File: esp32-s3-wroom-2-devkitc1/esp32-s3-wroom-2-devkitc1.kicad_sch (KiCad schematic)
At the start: 1 part

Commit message: net class plus cleanup
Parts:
- RFM95W1: footprint maciek-lib:lora-adafruit -> lora-adafruit
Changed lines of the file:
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@@
+		)
+	)
+	(netclass_flag ""
+		(length 2.54)
+		(shape round)
+		(at 107.95 88.9 0)
+		(fields_autoplaced yes)
+		(effects
+			(font
+				(size 1.27 1.27)
+			)
+			(justify left bottom)
+		)
+		(property "Netclass" "POWER"
+			(at 108.6485 86.36 0)
+			(effects
+				(font
+					(size 1.27 1.27)
+					(italic yes)
+				)
+				(justify left)
+			)
+		)
+	)
+	(netclass_flag ""
+		(length 2.54)
+		(shape round)
+		(at 107.95 86.36 0)
+		(fields_autoplaced yes)
+		(effects
+			(font
+				(size 1.27 1.27)
+			)
+			(justify left bottom)
+		)
+		(property "Netclass" "POWER"
+			(at 108.6485 83.82 0)
+			(effects
+				(font
+					(size 1.27 1.27)
+					(italic yes)
+				)
+				(justify left)
+			)
 		)
 	)
@@
 			)
 		)
-		(property "Footprint" "maciek-lib:lora-adafruit"
+		(property "Footprint" "lora-adafruit"
 			(at 132.08 106.68 0)
 			(effects

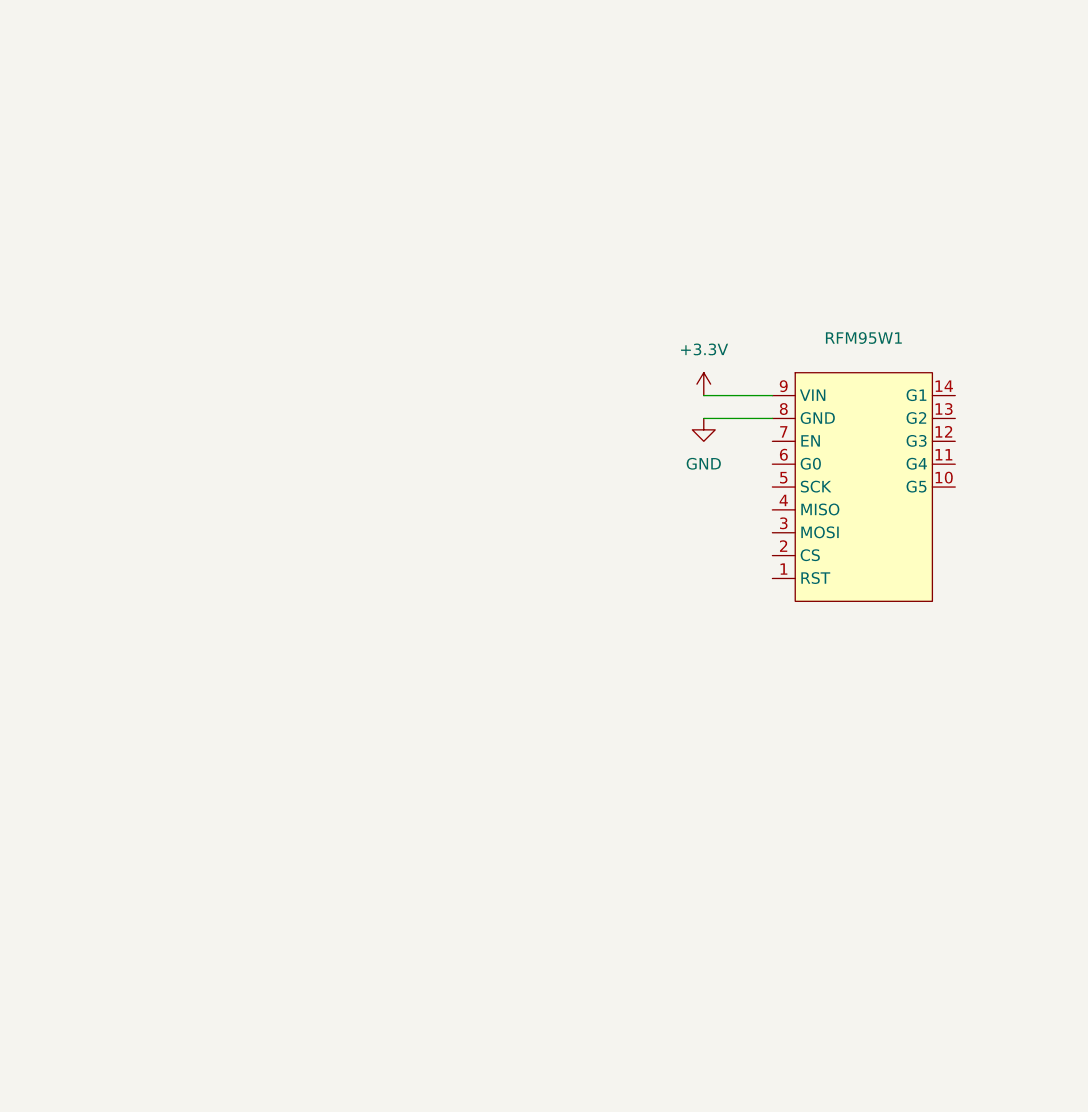
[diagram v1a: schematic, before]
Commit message: add nests and 3v3 area
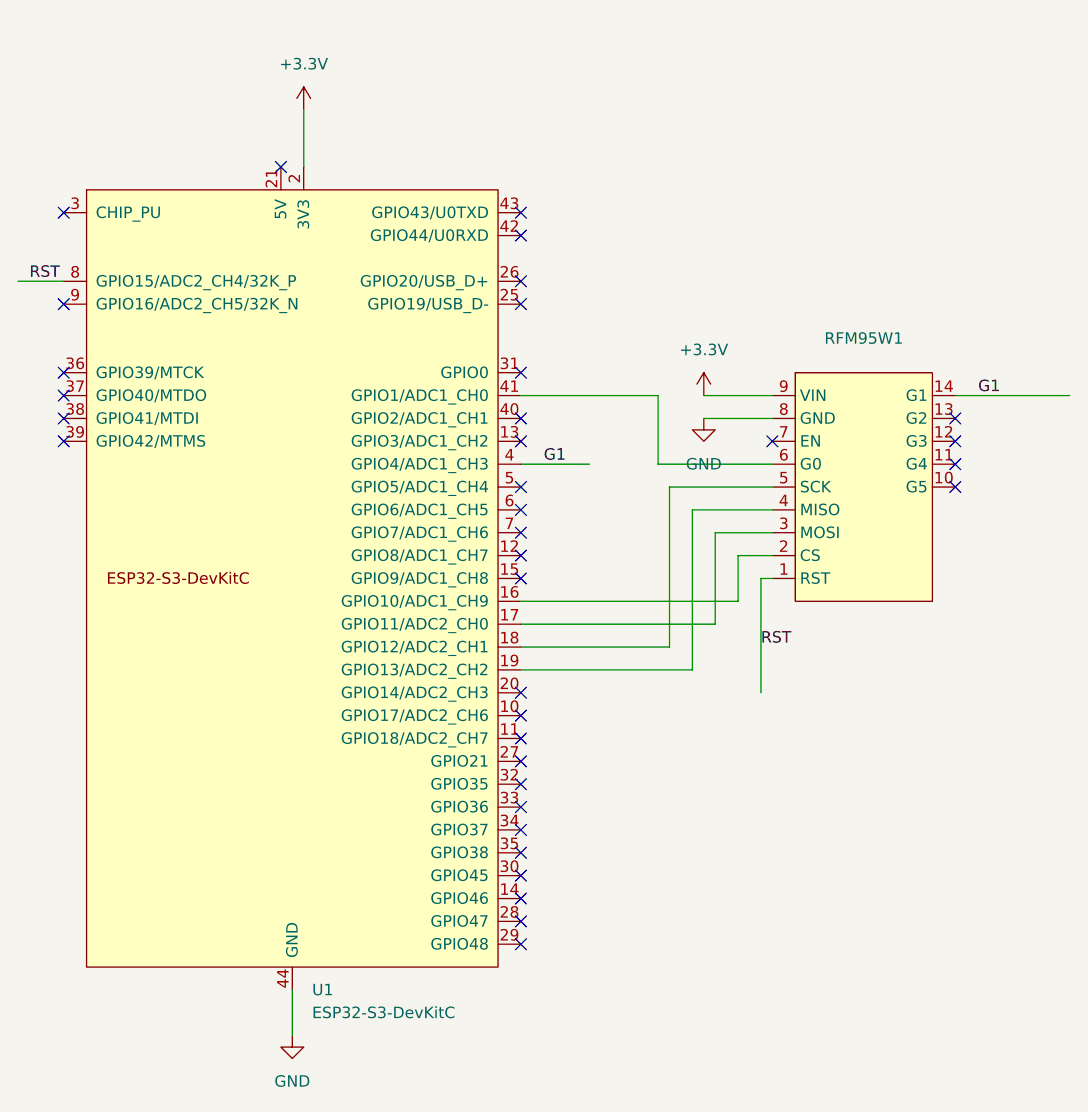
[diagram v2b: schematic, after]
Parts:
- added U1: ESP32-S3-DevKitC, PCM_Espressif:ESP32-S3-DevKitC, symbol PCM_Espressif:ESP32-S3-DevKitC
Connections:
- net +3.3V: now also U1.1 (3V3), U1.2 (3V3)
- net GND: now also U1.22 (GND), U1.23 (GND), U1.24 (GND), U1.44 (GND)
- net RST: now reaches RFM95W1.1 (RST)
- net RST: now also U1.8 (GPIO15/ADC2_CH4/32K_P)
- net G1: now reaches RFM95W1.14 (G1)
- net G1: now also U1.4 (GPIO4/ADC1_CH3)
- net at RFM95W1.2 (CS): now also U1.16 (GPIO10/ADC1_CH9)
- net at RFM95W1.3 (MOSI): now also U1.17 (GPIO11/ADC2_CH0)
- net at RFM95W1.4 (MISO): now also U1.19 (GPIO13/ADC2_CH2)
- net at RFM95W1.5 (SCK): now also U1.18 (GPIO12/ADC2_CH1)
- net at RFM95W1.6 (G0): now also U1.41 (GPIO1/ADC1_CH0)
- no-connect marks 0 -> 36

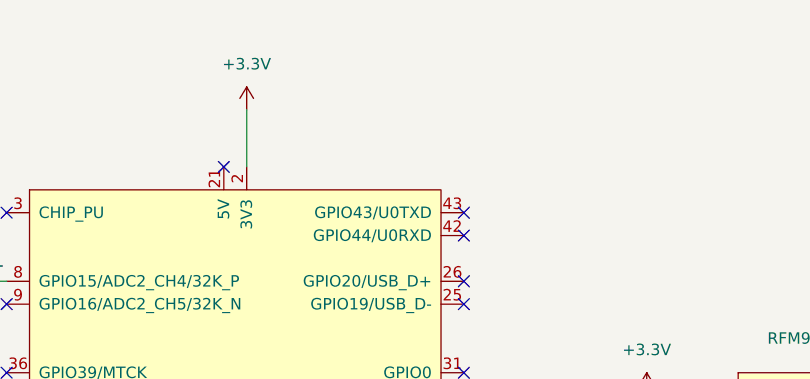
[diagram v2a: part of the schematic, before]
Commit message: need bigger holes
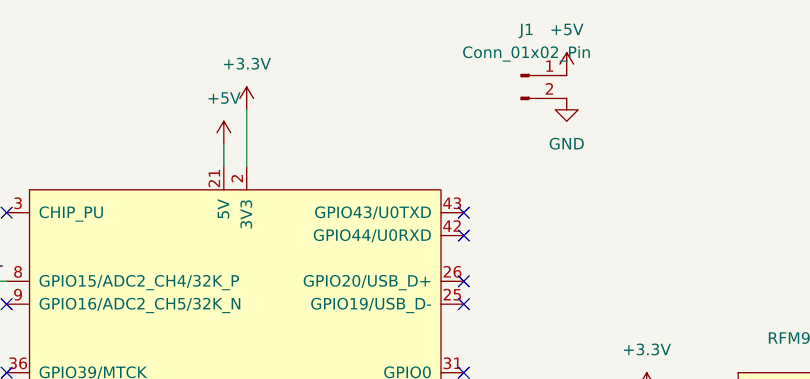
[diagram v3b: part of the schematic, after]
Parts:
- added J1: Conn_01x02_Pin, Connector_PinHeader_2.54mm:PinHeader_1x02_P2.54mm_Horizontal, symbol Connector:Conn_01x02_Pin
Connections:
- net GND: now also J1.2 (Pin_2)
- net +5V: now reaches U1.21 (5V)
- net +5V: now also J1.1 (Pin_1)
- no-connect marks 36 -> 35
